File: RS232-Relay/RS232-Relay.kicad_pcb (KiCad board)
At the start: 2 copper layers, 82.5 x 98.5 mm, 10 parts, among them J1 Conn_01x02, J2 Barrel_Jack, K3 Relay_DPDT, Q1 2N3904, U2 4N25

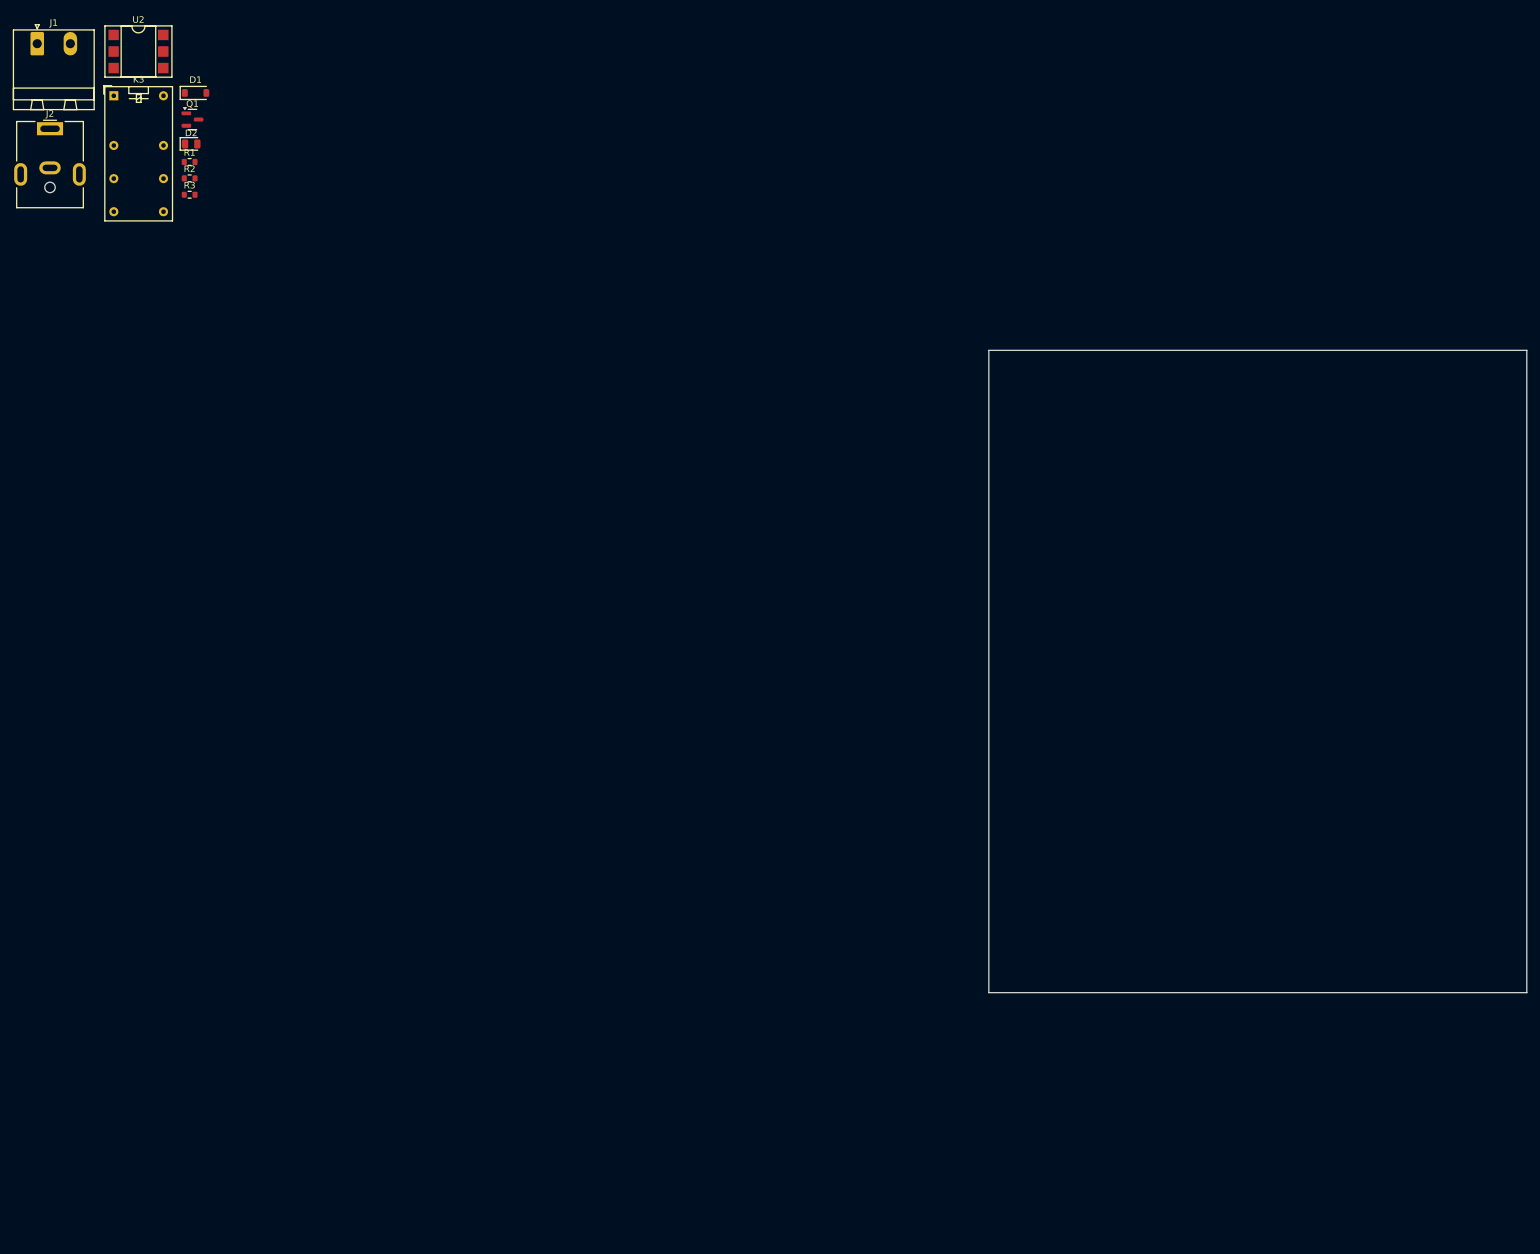
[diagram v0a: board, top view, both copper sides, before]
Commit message: Relay layout
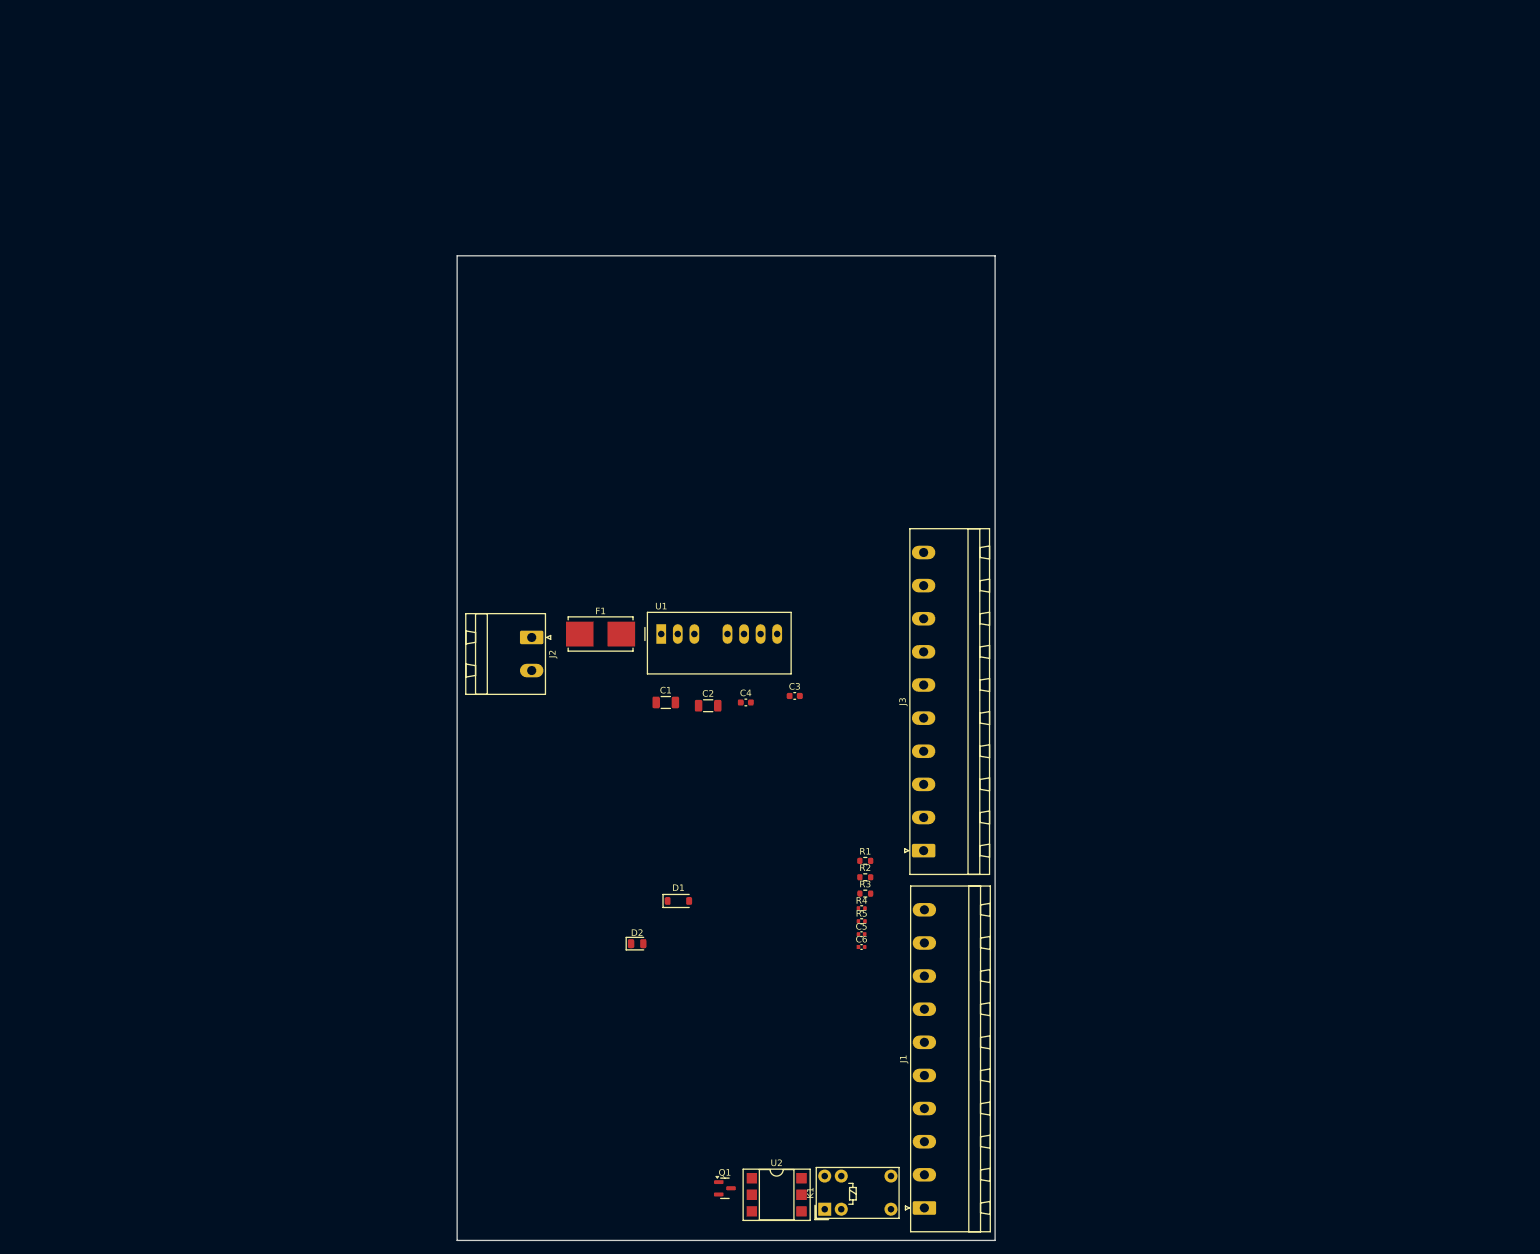
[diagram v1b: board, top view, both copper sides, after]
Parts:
- removed K3: Relay_DPDT, Relay_THT:Relay_DPDT_Omron_G5V-2
- added C1: 47u, Capacitor_SMD:C_1206_3216Metric, F.Cu at (100.5, 104.0)
- added C2: 47u, Capacitor_SMD:C_1206_3216Metric, F.Cu at (107.0, 104.5)
- added C3: 10u, Capacitor_SMD:C_0603_1608Metric, F.Cu at (120.2, 103.0)
- added C4: 10u, Capacitor_SMD:C_0603_1608Metric, F.Cu at (112.7, 104.0)
- added C5: 1u, Capacitor_SMD:C_0402_1005Metric, F.Cu at (130.5, 139.5)
- added C6: 1u, Capacitor_SMD:C_0402_1005Metric, F.Cu at (130.5, 141.5)
- added F1: 2A, Fuse:Fuseholder_Littelfuse_Nano2_154x, F.Cu at (90.5, 93.5)
- added J3: Conn_01x10, Connector_Phoenix_MSTB:PhoenixContact_MSTBA_2,5_10-G-5,08_1x10_P5.08mm_Horizontal, F.Cu at (140.0, 126.7)
- added K1: G5V-1, Relay_THT:Relay_SPDT_Omron_G5V-1, F.Cu at (124.8, 181.7)
- added R4: 10K, Resistor_SMD:R_0402_1005Metric, F.Cu at (130.5, 135.6)
- added R5: 10K, Resistor_SMD:R_0402_1005Metric, F.Cu at (130.5, 137.6)
- added U1: TEC2-1210WI, Converter_DCDC:Converter_DCDC_TRACO_TMR-xxxx_THT, F.Cu at (99.8, 93.5)
- J1: value Conn_01x02 -> Conn_01x10; footprint Connector_Phoenix_MSTB:PhoenixContact_MSTBA_2,5_2-G-5,08_1x02_P5.08mm_Horizontal -> Connector_Phoenix_MSTB:PhoenixContact_MSTBA_2,5_10-G-5,08_1x10_P5.08mm_Horizontal
- J2: value Barrel_Jack -> Conn_01x02; footprint Connector_BarrelJack:BarrelJack_CUI_PJ-063AH_Horizontal -> Connector_Phoenix_MSTB:PhoenixContact_MSTBA_2,5_2-G-5,08_1x02_P5.08mm_Horizontal
- moved J1 224.5 mm to (140.1, 181.5), turned to 90 degrees
- moved U2 200.8 mm to (117.5, 179.5)
- moved Q1 183.1 mm to (109.5, 178.5)
- moved R2 149.1 mm to (131.1, 130.8)
- moved R1 149.1 mm to (131.1, 128.3)
- moved R3 149.1 mm to (131.1, 133.3)
- moved D1 144.4 mm to (102.4, 134.4)
- moved D2 140.4 mm to (96.1, 141.0)
- moved J2 107.4 mm to (79.9, 94.0), turned to -90 degrees
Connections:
- net IN_1 renamed IN_01
- J1 pad 1: +12V -> RELAY_01
- J1 pad 2: Net-(J1-Pin_2) -> GND
- J2 pad 1: unconnected-(J2-Pad1) -> Net-(J2-Pin_1)
- J2 pad 2: unconnected-(J2-Pad2) -> GND
- U2 pad 2: GND -> GNDREF
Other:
- board size 82.5 x 98.5 mm -> 82.5 x 151 mm

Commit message: Adding RS232
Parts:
- removed C6: 1u, Capacitor_SMD:C_0402_1005Metric
- removed J1, J3: Conn_01x10, Connector_Phoenix_MSTB:PhoenixContact_MSTBA_2,5_10-G-5,08_1x10_P5.08mm_Horizontal
- removed R5: 10K, Resistor_SMD:R_0402_1005Metric
- added J4: Conn_01x09, Connector_PinHeader_2.54mm:PinHeader_1x09_P2.54mm_Vertical, F.Cu at (104.1, 45.7)
- added J5: Conn_01x09, Connector_PinHeader_2.54mm:PinHeader_1x09_P2.54mm_Vertical, F.Cu at (119.4, 45.7)
- added SW1: SW_SPST, Switch:PTS841, F.Cu at (98.6, 74.4)

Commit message: Basic schematic fully complete
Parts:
- removed C3, C4: 10u, Capacitor_SMD:C_0603_1608Metric
- removed C5: 1u, Capacitor_SMD:C_0402_1005Metric
- removed F1: 2A, Fuse:Fuseholder_Littelfuse_Nano2_154x
- removed SW1: SW_SPST, Switch:PTS841
- removed U2: 4N25, Package_DIP:DIP-6_W7.62mm_SMDSocket_SmallPads
- added C10: 0.1uF, Capacitor_SMD:C_0402_1005Metric, F.Cu at (110.1, 174.6)
- added C11: 0.1uF, Capacitor_SMD:C_0402_1005Metric, F.Cu at (113.0, 166.7)
- added C12: 1uF, Capacitor_SMD:C_0402_1005Metric, F.Cu at (113.0, 168.7)
- added C13: 0.1uF, Capacitor_SMD:C_0402_1005Metric, F.Cu at (113.0, 170.6)
- added C14: 1uF, Capacitor_SMD:C_0402_1005Metric, F.Cu at (113.0, 172.6)
- added C15: 1uF, Capacitor_SMD:C_0402_1005Metric, F.Cu at (113.0, 174.6)
- added C6: 0.1uF, Capacitor_SMD:C_0402_1005Metric, F.Cu at (110.1, 166.7)
- added C7: 1uF, Capacitor_SMD:C_0402_1005Metric, F.Cu at (110.1, 168.7)
- added C8: 0.1uF, Capacitor_SMD:C_0402_1005Metric, F.Cu at (110.1, 170.6)
- added C9: 0.1uF, Capacitor_SMD:C_0402_1005Metric, F.Cu at (110.1, 172.6)
- added D3: WS2812B, LED_SMD:LED_WS2812B_PLCC4_5.0x5.0mm_P3.2mm, F.Cu at (146.6, 94.7)
- added D4: WS2812B, LED_SMD:LED_WS2812B_PLCC4_5.0x5.0mm_P3.2mm, F.Cu at (146.9, 119.7)
- added D5: Green, LED_SMD:LED_0805_2012Metric, F.Cu at (116.2, 142.5)
- added D6: Green, LED_SMD:LED_0805_2012Metric, F.Cu at (116.2, 145.6)
- added D7: Green, LED_SMD:LED_0805_2012Metric, F.Cu at (116.2, 148.6)
- added J1: Relay 1-4, Connector_Phoenix_MSTB:PhoenixContact_MSTBA_2,5_8-G-5,08_1x08_P5.08mm_Horizontal, F.Cu at (85.5, 40.5)
- added J3: Relay 5-8, Connector_Phoenix_MSTB:PhoenixContact_MSTBA_2,5_8-G-5,08_1x08_P5.08mm_Horizontal, F.Cu at (85.5, 93.3)
- added J6: Relay 9-12, Connector_Phoenix_MSTB:PhoenixContact_MSTBA_2,5_8-G-5,08_1x08_P5.08mm_Horizontal, F.Cu at (85.5, 146.0)
- added J7: RS232_1, Connector_Phoenix_MSTB:PhoenixContact_MSTBA_2,5_3-G-5,08_1x03_P5.08mm_Horizontal, F.Cu at (138.5, 52.0)
- added J8: RS232_2, Connector_Phoenix_MSTB:PhoenixContact_MSTBA_2,5_3-G-5,08_1x03_P5.08mm_Horizontal, F.Cu at (138.5, 70.7)
- added R10: 50R, Resistor_SMD:R_0603_1608Metric, F.Cu at (96.0, 148.3)
- added R5: 220R, Resistor_SMD:R_0603_1608Metric, F.Cu at (96.0, 140.8)
- added R6: 10K, Resistor_SMD:R_0402_1005Metric, F.Cu at (106.2, 146.0)
- added R7: 10K, Resistor_SMD:R_0402_1005Metric, F.Cu at (106.2, 148.0)
- added R8: 4K7, Resistor_SMD:R_0603_1608Metric, F.Cu at (96.0, 143.3)
- added R9: 220R, Resistor_SMD:R_0603_1608Metric, F.Cu at (96.0, 145.8)
- added SW2: SW_SPST, Switch:PTS841, F.Cu at (148.8, 103.0)
- added SW3: SW_SPST, Switch:PTS841, F.Cu at (148.6, 109.5)
- added TP1: 3V3, TestPoint:TestPoint_Pad_D1.0mm, F.Cu at (92.0, 154.0)
- added TP10: I2C_SCL, TestPoint:TestPoint_Pad_D1.0mm, F.Cu at (95.0, 166.2)
- added TP11: I2C_INT, TestPoint:TestPoint_Pad_D1.0mm, F.Cu at (98.0, 154.0)
- added TP12: BTN_01, TestPoint:TestPoint_Pad_D1.0mm, F.Cu at (98.0, 157.1)
- added TP13: BTN_02, TestPoint:TestPoint_Pad_D1.0mm, F.Cu at (98.0, 160.1)
- added TP2: Signal In, TestPoint:TestPoint_Pad_D1.0mm, F.Cu at (92.0, 157.1)
- added TP3: Signal Out, TestPoint:TestPoint_Pad_D1.0mm, F.Cu at (92.0, 160.1)
- added TP4: GND_ISO, TestPoint:TestPoint_Pad_D1.0mm, F.Cu at (92.0, 163.2)
- added TP5: UART_1_TX, TestPoint:TestPoint_Pad_D1.0mm, F.Cu at (92.0, 166.2)
- added TP6: UART_1_RX, TestPoint:TestPoint_Pad_D1.0mm, F.Cu at (95.0, 154.0)
- added TP7: UART_2_TX, TestPoint:TestPoint_Pad_D1.0mm, F.Cu at (95.0, 157.1)
- added TP8: UART_2_RX, TestPoint:TestPoint_Pad_D1.0mm, F.Cu at (95.0, 160.1)
- added TP9: I2C_SDA, TestPoint:TestPoint_Pad_D1.0mm, F.Cu at (95.0, 163.2)
- added U3: PCF8575DBR, Package_SO:SSOP-24_5.3x8.2mm_P0.65mm, F.Cu at (113.5, 111.0)
- added U4: MAX3232, Package_SO:TSSOP-16_4.4x5mm_P0.65mm, F.Cu at (128.8, 72.2)
- C1, C2: value 47u -> 10u; footprint Capacitor_SMD:C_1206_3216Metric -> Capacitor_SMD:C_0603_1608Metric
- D1: value D -> 1N4148W
- D2: value LED -> RED
- R1: value 470R -> 1000R
- R2: value 330R -> 1000R
- R4: value 10K -> 4K7; footprint Resistor_SMD:R_0402_1005Metric -> Resistor_SMD:R_0603_1608Metric
- moved K1 141.0 mm to (114.1, 41.1), turned to -90 degrees
- moved J2 104.7 mm to (139.0, 180.5), turned to 90 degrees
- moved D2 87.5 mm to (106.8, 54.2), turned to 90 degrees
- moved R2 77.1 mm to (106.5, 57.7), turned to -90 degrees
- moved U1 74.2 mm to (126.7, 162.6)
- moved J4 57.2 mm to (121.0, 100.3)
- moved J5 57.2 mm to (136.2, 100.3)
- moved R1 41.8 mm to (92.0, 143.3)
- moved R3 41.8 mm to (92.0, 148.3)
- moved C2 39.3 mm to (92.0, 140.8)
- moved Q1 35.8 mm to (107.2, 142.8)
- moved C1 35.3 mm to (92.0, 138.3)
- moved R4 34.6 mm to (96.0, 138.3)
- moved D1 6.76 mm to (107.6, 138.7)
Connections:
- C2 pad 1: +3V3 -> +12V
- C2 pad 2: GNDREF -> GND
- J2 pad 1: Net-(J2-Pin_1) -> +12V
- J5 pad 8: ESP32_GPIO_21 -> BTN_01
- J5 pad 9: ESP32_GPIO_22 -> BTN_02
- R1 pad 1: IN_01 -> +12V
- R4 pad 1: +3V3 -> ESP32_GPIO_04
- R4 pad 2: ESP_BTN_01 -> +3V3

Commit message: Fixing pin headers
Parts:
- removed D3, D4: WS2812B, LED_SMD:LED_WS2812B_PLCC4_5.0x5.0mm_P3.2mm
- added U2: 4N25, Package_DIP:DIP-6_W7.62mm_SMDSocket_SmallPads, F.Cu at (116.2, 71.0)
- added U5: LTV-847S, Package_DIP:SMDIP-16_W9.53mm, F.Cu at (103.7, 77.3)

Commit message: Schematic complete
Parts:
- removed D1: 1N4148W, Diode_SMD:D_SOD-123
- removed D2: RED, LED_SMD:LED_0805_2012Metric
- removed K1: G5V-1, Relay_THT:Relay_SPDT_Omron_G5V-1
- removed Q1: 2N3904, Package_TO_SOT_SMD:SOT-23
- removed R2: 1000R, Resistor_SMD:R_0603_1608Metric
- removed R3, R5: 220R, Resistor_SMD:R_0603_1608Metric
- removed TP2: Signal In, TestPoint:TestPoint_Pad_D1.0mm
- removed TP3: Signal Out, TestPoint:TestPoint_Pad_D1.0mm
- removed U2: 4N25, Package_DIP:DIP-6_W7.62mm_SMDSocket_SmallPads
- removed U5: LTV-847S, Package_DIP:SMDIP-16_W9.53mm
- J4, J5: footprint Connector_PinHeader_2.54mm:PinHeader_1x09_P2.54mm_Vertical -> Connector_PinSocket_2.54mm:PinSocket_1x09_P2.54mm_Vertical

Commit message: Pre-template layouts
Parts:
- removed J1: Relay 1-4, Connector_Phoenix_MSTB:PhoenixContact_MSTBA_2,5_8-G-5,08_1x08_P5.08mm_Horizontal
- removed J3: Relay 5-8, Connector_Phoenix_MSTB:PhoenixContact_MSTBA_2,5_8-G-5,08_1x08_P5.08mm_Horizontal
- removed J6: Relay 9-12, Connector_Phoenix_MSTB:PhoenixContact_MSTBA_2,5_8-G-5,08_1x08_P5.08mm_Horizontal
- added D1: RED, LED_SMD:LED_0805_2012Metric, F.Cu at (103.5, 60.0)
- added D10: RED, LED_SMD:LED_0805_2012Metric, F.Cu at (50.2, 69.7)
- added D11: 1N4148W, Diode_SMD:D_SOD-123, F.Cu at (45.1, 64.7)
- added D12: RED, LED_SMD:LED_0805_2012Metric, F.Cu at (-66.5, 65.5)
- added D13: RED, LED_SMD:LED_0805_2012Metric, F.Cu at (-66.5, 68.5)
- added D14: 1N4148W, Diode_SMD:D_SOD-123, F.Cu at (-71.7, 65.6)
- added D15: 1N4148W, Diode_SMD:D_SOD-123, F.Cu at (-71.7, 69.0)
- added D16: RED, LED_SMD:LED_0805_2012Metric, F.Cu at (-66.5, 71.6)
- added D17: RED, LED_SMD:LED_0805_2012Metric, F.Cu at (-66.5, 74.6)
- added D18: 1N4148W, Diode_SMD:D_SOD-123, F.Cu at (-71.7, 72.3)
- added D19: 1N4148W, Diode_SMD:D_SOD-123, F.Cu at (-71.7, 75.7)
- added D2: 1N4148W, Diode_SMD:D_SOD-123, F.Cu at (103.0, 63.5)
- added D20: RED, LED_SMD:LED_0805_2012Metric, F.Cu at (-19.9, 65.5)
- added D21: RED, LED_SMD:LED_0805_2012Metric, F.Cu at (-19.9, 68.5)
- added D22: 1N4148W, Diode_SMD:D_SOD-123, F.Cu at (-25.0, 65.6)
- added D23: 1N4148W, Diode_SMD:D_SOD-123, F.Cu at (-25.0, 69.0)
- added D24: RED, LED_SMD:LED_0805_2012Metric, F.Cu at (-19.9, 71.6)
- added D25: RED, LED_SMD:LED_0805_2012Metric, F.Cu at (-19.9, 74.6)
- added D26: 1N4148W, Diode_SMD:D_SOD-123, F.Cu at (-25.0, 72.3)
- added D27: 1N4148W, Diode_SMD:D_SOD-123, F.Cu at (-25.0, 75.7)
- added D3: RED, LED_SMD:LED_0805_2012Metric, F.Cu at (50.2, 63.6)
- added D4: 1N4148W, Diode_SMD:D_SOD-123, F.Cu at (45.1, 58.0)
- added D8: RED, LED_SMD:LED_0805_2012Metric, F.Cu at (50.2, 66.6)
- added D9: 1N4148W, Diode_SMD:D_SOD-123, F.Cu at (45.1, 61.3)
- added J10: Relay 1-4, Connector_Phoenix_MSTB:PhoenixContact_MSTBA_2,5_8-G-5,08_1x08_P5.08mm_Horizontal, F.Cu at (85.5, 146.0)
- added J11: Relay 1-4, Connector_Phoenix_MSTB:PhoenixContact_MSTBA_2,5_8-G-5,08_1x08_P5.08mm_Horizontal, F.Cu at (85.5, 93.2)
- added J9: Relay 1-4, Connector_Phoenix_MSTB:PhoenixContact_MSTBA_2,5_8-G-5,08_1x08_P5.08mm_Horizontal, F.Cu at (85.5, 40.5)
- added K1: G5V-1, Relay_THT:Relay_SPDT_Omron_G5V-1, F.Cu at (100.0, 60.8)
- added K10: G5V-1, Relay_THT:Relay_SPDT_Omron_G5V-1, F.Cu at (-34.6, 52.0)
- added K11: G5V-1, Relay_THT:Relay_SPDT_Omron_G5V-1, F.Cu at (-25.5, 52.0)
- added K12: G5V-1, Relay_THT:Relay_SPDT_Omron_G5V-1, F.Cu at (-16.4, 52.0)
- added K2: G5V-1, Relay_THT:Relay_SPDT_Omron_G5V-1, F.Cu at (100.0, 40.4)
- added K3: G5V-1, Relay_THT:Relay_SPDT_Omron_G5V-1, F.Cu at (100.0, 50.5)
- added K4: G5V-1, Relay_THT:Relay_SPDT_Omron_G5V-1, F.Cu at (100.0, 71.0)
- added K5: G5V-1, Relay_THT:Relay_SPDT_Omron_G5V-1, F.Cu at (-90.5, 52.0)
- added K6: G5V-1, Relay_THT:Relay_SPDT_Omron_G5V-1, F.Cu at (-81.3, 52.0)
- added K7: G5V-1, Relay_THT:Relay_SPDT_Omron_G5V-1, F.Cu at (-72.2, 52.0)
- added K8: G5V-1, Relay_THT:Relay_SPDT_Omron_G5V-1, F.Cu at (-63.1, 52.0)
- added K9: G5V-1, Relay_THT:Relay_SPDT_Omron_G5V-1, F.Cu at (-43.8, 52.0)
- added Q1: 2N3904, Package_TO_SOT_SMD:SOT-23, F.Cu at (106.4, 64.8)
- added Q10: 2N3904, Package_TO_SOT_SMD:SOT-23, F.Cu at (-30.3, 71.0)
- added Q11: 2N3904, Package_TO_SOT_SMD:SOT-23, F.Cu at (-30.3, 75.6)
- added Q12: 2N3904, Package_TO_SOT_SMD:SOT-23, F.Cu at (-30.3, 80.2)
- added Q2: 2N3904, Package_TO_SOT_SMD:SOT-23, F.Cu at (39.7, 60.0)
- added Q3: 2N3904, Package_TO_SOT_SMD:SOT-23, F.Cu at (39.7, 64.6)
- added Q4: 2N3904, Package_TO_SOT_SMD:SOT-23, F.Cu at (39.7, 69.2)
- added Q5: 2N3904, Package_TO_SOT_SMD:SOT-23, F.Cu at (-77.0, 66.4)
- added Q6: 2N3904, Package_TO_SOT_SMD:SOT-23, F.Cu at (-77.0, 71.0)
- added Q7: 2N3904, Package_TO_SOT_SMD:SOT-23, F.Cu at (-77.0, 75.6)
- added Q8: 2N3904, Package_TO_SOT_SMD:SOT-23, F.Cu at (-77.0, 80.2)
- added Q9: 2N3904, Package_TO_SOT_SMD:SOT-23, F.Cu at (-30.3, 66.4)
- added R11: 1000R, Resistor_SMD:R_0603_1608Metric, F.Cu at (54.4, 67.8)
- added R12: 220R, Resistor_SMD:R_0603_1608Metric, F.Cu at (58.4, 60.3)
- added R13: 660R, Resistor_SMD:R_0603_1608Metric, F.Cu at (58.4, 62.8)
- added R14: 1000R, Resistor_SMD:R_0603_1608Metric, F.Cu at (58.4, 65.3)
- added R15: 220R, Resistor_SMD:R_0603_1608Metric, F.Cu at (58.4, 67.8)
- added R16: 660R, Resistor_SMD:R_0603_1608Metric, F.Cu at (51.4, 56.0)
- added R17: 1000R, Resistor_SMD:R_0603_1608Metric, F.Cu at (62.5, 62.8)
- added R18: 220R, Resistor_SMD:R_0603_1608Metric, F.Cu at (62.5, 65.3)
- added R19: 660R, Resistor_SMD:R_0603_1608Metric, F.Cu at (62.5, 67.8)
- added R2: 1000R, Resistor_SMD:R_0603_1608Metric, F.Cu at (106.8, 60.0)
- added R20: 1000R, Resistor_SMD:R_0603_1608Metric, F.Cu at (-62.3, 65.2)
- added R21: 220R, Resistor_SMD:R_0603_1608Metric, F.Cu at (-62.3, 67.7)
- added R22: 1000R, Resistor_SMD:R_0603_1608Metric, F.Cu at (-62.3, 70.2)
- added R23: 220R, Resistor_SMD:R_0603_1608Metric, F.Cu at (-62.3, 72.7)
- added R24: 660R, Resistor_SMD:R_0603_1608Metric, F.Cu at (-58.3, 65.2)
- added R25: 660R, Resistor_SMD:R_0603_1608Metric, F.Cu at (-58.3, 67.7)
- added R26: 1000R, Resistor_SMD:R_0603_1608Metric, F.Cu at (-58.3, 70.2)
- added R27: 1000R, Resistor_SMD:R_0603_1608Metric, F.Cu at (-58.3, 72.7)
- added R28: 220R, Resistor_SMD:R_0603_1608Metric, F.Cu at (-54.3, 65.2)
- added R29: 220R, Resistor_SMD:R_0603_1608Metric, F.Cu at (-54.3, 67.7)
- added R3: 220R, Resistor_SMD:R_0603_1608Metric, F.Cu at (54.4, 62.8)
- added R30: 660R, Resistor_SMD:R_0603_1608Metric, F.Cu at (-54.3, 70.2)
- added R31: 660R, Resistor_SMD:R_0603_1608Metric, F.Cu at (-54.3, 72.7)
- added R32: 1000R, Resistor_SMD:R_0603_1608Metric, F.Cu at (-15.6, 65.2)
- added R33: 220R, Resistor_SMD:R_0603_1608Metric, F.Cu at (-15.6, 67.7)
- added R34: 1000R, Resistor_SMD:R_0603_1608Metric, F.Cu at (-15.6, 70.2)
- added R35: 220R, Resistor_SMD:R_0603_1608Metric, F.Cu at (-15.6, 72.7)
- added R36: 660R, Resistor_SMD:R_0603_1608Metric, F.Cu at (-11.6, 65.2)
- added R37: 660R, Resistor_SMD:R_0603_1608Metric, F.Cu at (-11.6, 67.7)
- added R38: 1000R, Resistor_SMD:R_0603_1608Metric, F.Cu at (-11.6, 70.2)
- added R39: 1000R, Resistor_SMD:R_0603_1608Metric, F.Cu at (-11.6, 72.7)
- added R40: 220R, Resistor_SMD:R_0603_1608Metric, F.Cu at (-7.62, 65.2)
- added R41: 220R, Resistor_SMD:R_0603_1608Metric, F.Cu at (-7.62, 67.7)
- added R42: 660R, Resistor_SMD:R_0603_1608Metric, F.Cu at (-7.62, 70.2)
- added R43: 660R, Resistor_SMD:R_0603_1608Metric, F.Cu at (-7.62, 72.7)
- added R5: 660R, Resistor_SMD:R_0603_1608Metric, F.Cu at (107.0, 62.0)
- added U2: LTV-847S, Package_DIP:SMDIP-16_W9.53mm, F.Cu at (116.0, 61.5)
- added U6: LTV-847S, Package_DIP:SMDIP-16_W9.53mm, F.Cu at (-86.0, 74.9)
- added U7: LTV-847S, Package_DIP:SMDIP-16_W9.53mm, F.Cu at (-39.4, 74.9)
- moved C9 102.1 mm to (143.8, 76.2), turned to 90 degrees
- moved C7 97.9 mm to (142.6, 76.3), turned to 90 degrees
- moved C10 96.9 mm to (133.4, 80.5), turned to 90 degrees
- moved C8 95.0 mm to (133.4, 78.5), turned to 90 degrees
- moved C11 94.5 mm to (135.0, 74.8)
- moved C6 93.1 mm to (133.4, 76.5), turned to -90 degrees
- moved C1 81.8 mm to (164.2, 100.0)
- moved C12 81.8 mm to (185.3, 130.4)
- moved C13 81.8 mm to (185.3, 132.4)
- moved C2 81.8 mm to (164.2, 102.5)
- moved D6 81.8 mm to (188.5, 107.3)
- moved D7 81.8 mm to (188.5, 110.3)
- moved R1 81.8 mm to (164.2, 105.0)
- moved R4 81.8 mm to (168.3, 100.0)
- moved R9 81.8 mm to (168.3, 107.5)
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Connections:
- net ESP32_GPIO_00 renamed /ESP_32_GPIO_00
- net ESP32_GPIO_01 renamed /ESP_32_GPIO_01
- net ESP32_GPIO_02 renamed /ESP_32_GPIO_02
- net ESP32_GPIO_03 renamed I2C_SDA
- net ESP32_GPIO_04 renamed I2C_SCL
- net ESP32_GPIO_05 renamed I2C_INT
- net ESP32_GPIO_14 renamed UART_2_TX
- net ESP32_GPIO_15 renamed UART_2_RX
- net ESP32_GPIO_18 renamed /ESP_32_GPIO_18
- net ESP32_GPIO_19 renamed /ESP_32_GPIO_19
- net ESP32_GPIO_20 renamed /ESP_32_GPIO_20
- net ESP32_UART0_RX renamed UART_1_RX
- net ESP32_UART0_TX renamed UART_1_TX
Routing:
- net +12V: track 0.00 -> 32.6 mm
- net Net-(D2-A): track 0.00 -> 17.6 mm
- net /Relay-Module/RELAY_OUT_02: track 0.00 -> 9.48 mm
- net /Relay-Module/RELAY_OUT_01: track 0.00 -> 9.45 mm
- net /Relay-Module/RELAY_OUT_03: track 0.00 -> 9.45 mm
- net /Relay-Module/RELAY_OUT_04: track 0.00 -> 9.43 mm
- net Net-(R5-Pad1): track 0.00 -> 6.56 mm
- net Net-(U4-VS+): track 0.00 -> 3.12 mm
- net +3V3: track 0.00 -> 2.97 mm
- net GNDREF: track 0.00 -> 2.95 mm
- net Net-(Q1-B): track 0.00 -> 2.32 mm
- net Net-(U4-VS-): track 0.00 -> 2.09 mm
- net Net-(U4-C2-): track 0.00 -> 1.93 mm
- net GND: track 0.00 -> 1.93 mm, vias 0 -> 1
- net Net-(U4-C1-): track 0.00 -> 1.84 mm
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- added copper zone on B.Cu, net GND
- added copper zone on B.Cu, net GNDREF
- added copper zone on F.Cu, net GNDREF
